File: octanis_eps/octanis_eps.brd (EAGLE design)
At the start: 100 x 80 mm, 167 parts, among them IC10 OPA2333DGK, IC11 OPA2333DGK, IC12 OPA2333DGK, IC2 OPA2333DGK, IC3 OPA2333DGK, IC4 OPA2333DGK, IC5 OPA2333DGK, IC6 OPA2333DGK, IC7 OPA2333DGK, IC8 OPA2333DGK, IC9 OPA2333DGK, Q1 FC-12M

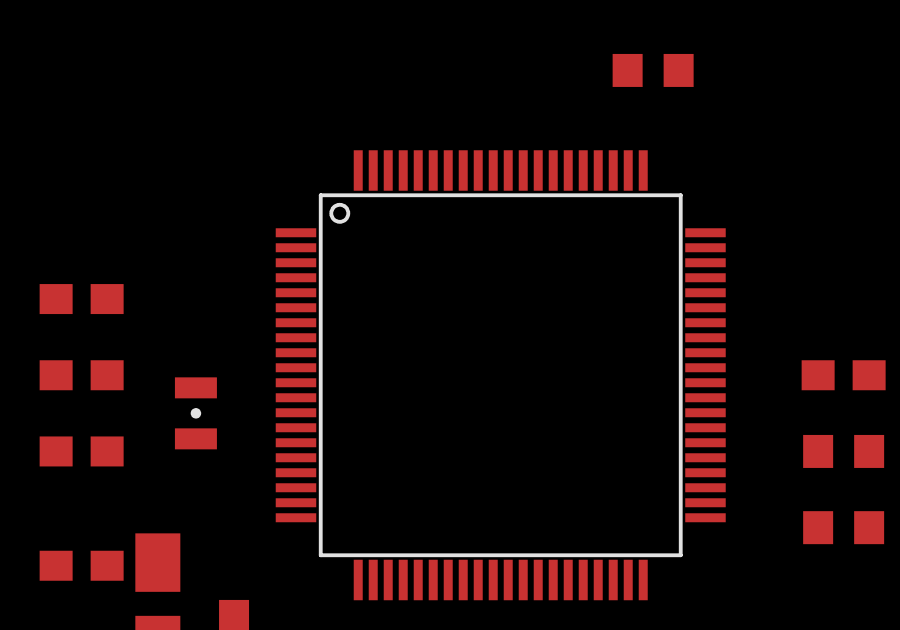
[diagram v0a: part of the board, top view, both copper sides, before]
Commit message: replaced the msp430 to the same component like in the octanis 0.1 board
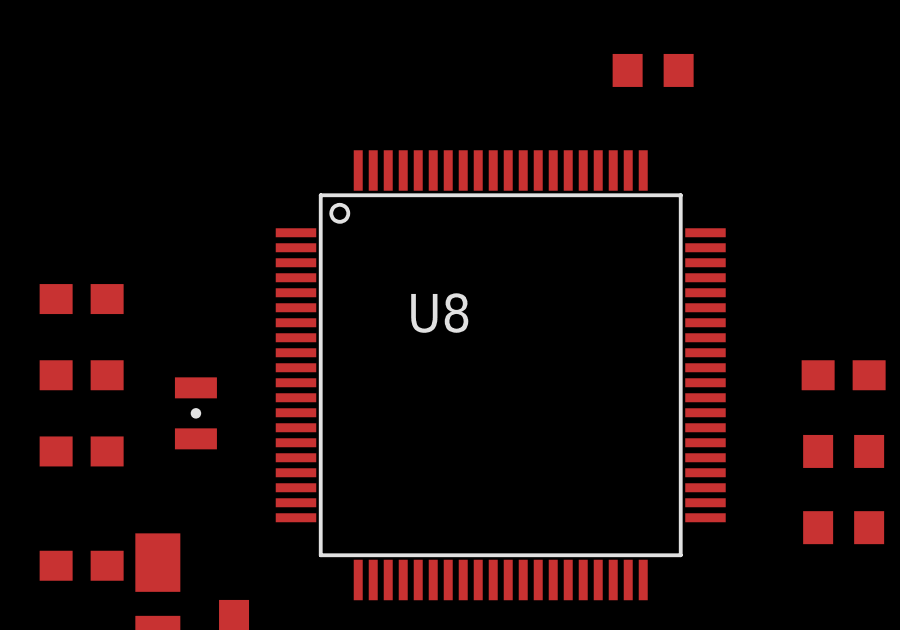
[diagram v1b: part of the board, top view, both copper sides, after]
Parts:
- removed U$1: F552X---PN80, TI_MSP430_v16:PN80
- added U8: MSP430F5529IPNR, TI_MSP430_v16_intern:PN80
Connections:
- net +3V3: now also U8.14, U8.18, U8.50; no longer U$1.14, U$1.18, U$1.50
- net 65: now also U8.65; no longer U$1.65
- net 66: now also U8.66; no longer U$1.66
- net 67: now also U8.67; no longer U$1.67
- net GND: now also U8.19, U8.49, U8.61, U8.68; no longer U$1.19, U$1.49, U$1.61, U$1.68
- net I2C_SCL: now also U8.47; no longer U$1.47
- net I2C_SDA: now also U8.46; no longer U$1.46
- net I_BOT_MS: now also U8.78; no longer U$1.78
- net I_CHG_MS: now also U8.79; no longer U$1.79
- net I_DSG_MS: now also U8.80; no longer U$1.80
- net I_TOP_MS: now also U8.77; no longer U$1.77
- net N$27: now also U8.63; no longer U$1.63
- net N$28: now also U8.45; no longer U$1.45
- net N$34: now also U8.3; no longer U$1.3
- net N$35: now also U8.4; no longer U$1.4
- net N$48: now also U8.12; no longer U$1.12
- net N$49: now also U8.20; no longer U$1.20
- net N$50: now also U8.13; no longer U$1.13
- net RST/SBWTDIO: now also U8.76; no longer U$1.76
- net TEST/SBWTCK: now also U8.71; no longer U$1.71
- net VCC: now also U8.11; no longer U$1.11
- net V_BT_MS: now also U8.2; no longer U$1.2
- net V_BUS_MS: now also U8.1; no longer U$1.1

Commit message: eps board save Thu-22-01-2015
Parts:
- removed EXT1, EXT2: (no value), jumper:JP4
- removed JP1, JP2, JP3, JP4, JP5: (no value), jumper:JP1
- removed U8: MSP430F5529IPNR, TI_MSP430_v16_intern:PN80
- added A_EXT, PW_EXT1, PW_EXT2, PW_EXT3, SC_JMPR: (no value), jumper:JP4
- added I2C: (no value), jumper:JP1
- added U$1: F552X---PN80, TI_MSP430_v16:PN80
- added U$16, U$17, U$18: TPS2022D, Octanis1_EPS:SO8
- moved U$15 508.6 mm to (54.6, 54.6), flipped to the bottom
- moved U$14 503.2 mm to (61.0, 54.6), flipped to the bottom
- moved U$13 492.2 mm to (48.3, 54.6), flipped to the bottom
- moved U$8 33.2 mm to (35.6, 33.0)
- moved LTC3411 30.9 mm to (80.0, 26.7)
- moved C17 30.5 mm to (91.4, 14.0)
- moved C9 21.6 mm to (81.3, 19.1)
- moved R68 17.3 mm to (83.8, 15.2)
- moved JP7 14.2 mm to (76.2, 76.2), turned to 0 degrees
- moved IC11 10.5 mm to (77.5, 12.7)
- moved IC10 9.67 mm to (80.0, 6.35)
- moved L1 8.98 mm to (88.9, 27.9)
- moved BT_JMPR 4.26 mm to (31.1, 72.4), turned to 90 degrees
- moved R10 3.81 mm to (38.1, 71.1)
- moved C7 1.80 mm to (29.2, 59.7)
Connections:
- removed net I_BOT_MS: IC3.6, IC3.7, U8.78
- removed net I_TOP_MS: IC3.1, IC3.2, U8.77
- removed net N$35: U8.4
- removed net SC+_BOT: R8.1, SC_BOT.1, SC_BOT.2, U$2.8
- removed net SC+_TOP: R6.1, SC_TOP.1, SC_TOP.2, U$3.8
- new net AEXT4: A_EXT.1, U$1.6
- new net A_EXT1: A_EXT.4, U$1.3
- new net A_EXT2: A_EXT.3, U$1.4
- new net A_EXT3: A_EXT.2, U$1.5
- new net EN_EXT1: U$1.57, U$13.1
- new net EN_EXT2: U$1.58, U$15.1
- new net EN_EXT3: U$1.59, U$14.1
- new net EXT3+: PW_EXT3.3, PW_EXT3.4, U$18.6, U$18.7, U$18.8
- new net EXT_PW: C26.+, C27.+, C28.+, C29.2, C30.2, C31.2, R6.2, U$16.2, U$16.3, U$17.2, U$17.3, U$18.2, U$18.3, U$3.6
- new net I_EXT_PW: IC3.1, IC3.2, U$1.78
- new net I_SC: IC3.6, IC3.7, U$1.77
- new net N$79: U$13.3, U$16.4
- new net N$80: U$14.3, U$18.4
- new net SC+: R8.1, SC_BOT.1, SC_BOT.2, SC_TOP.1, SC_TOP.2, U$2.8
- new net SC-: SC_BOT.3, SC_BOT.4, SC_JMPR.2, SC_JMPR.4, SC_TOP.3, SC_TOP.4
- net +3V3: now also U$1.14, U$1.18, U$1.50; no longer U8.14, U8.18, U8.50
- net 65: now also U$1.65; no longer U8.65
- net 66: now also U$1.66; no longer U8.66
- net 67: now also U$1.67; no longer U8.67
- net EXT1+: now also PW_EXT1.3, PW_EXT1.4, U$16.6, U$16.7, U$16.8; no longer EXT1.3, EXT1.4
- net EXT2+: now also PW_EXT2.3, PW_EXT2.4, U$17.6, U$17.7, U$17.8; no longer EXT2.3, EXT2.4
- net GND: now also C26.-, C27.-, C28.-, C29.1, C30.1, C31.1, PW_EXT1.1, PW_EXT1.2, PW_EXT2.1, PW_EXT2.2, PW_EXT3.1, PW_EXT3.2, SC_JMPR.1, SC_JMPR.3, U$1.19, U$1.49, U$1.61, U$1.68, U$16.1, U$17.1, U$18.1; no longer EXT1.1, EXT1.2, EXT2.1, EXT2.2, SC_BOT.3, SC_BOT.4, SC_TOP.3, SC_TOP.4, U8.19, U8.49, U8.61, U8.68
- net I2C_SCL: now also I2C.1, U$1.47; no longer JP1.1, U8.47
- net I2C_SDA: now also I2C.2, U$1.46; no longer JP1.2, U8.46
- net I_CHG_MS: now also U$1.79; no longer U8.79
- net I_DSG_MS: now also U$1.80; no longer U8.80
- net N$27: now also U$1.63; no longer U8.63
- net N$28: now also U$1.45; no longer U8.45
- net N$34: now also U$15.3, U$17.4; no longer U8.3
- net N$48: now also U$1.12; no longer U8.12
- net N$49: now also U$1.20; no longer U8.20
- net N$50: now also U$1.13; no longer U8.13
- net RST/SBWTDIO: now also U$1.76; no longer U8.76
- net TEST/SBWTCK: now also U$1.71; no longer U8.71
- net VCC: now also R6.1, U$1.11, U$3.8; no longer R6.2, U$3.6, U8.11
- net V_BT_MS: now also U$1.2; no longer U8.2
- net V_BUS_MS: now also U$1.1; no longer U8.1
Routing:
- net EXT_PW: track 0.00 -> 51.8 mm, vias 0 -> 1
- net SC-: track 0.00 -> 30.0 mm
- net SC+: track 0.00 -> 10.3 mm
- net BT_IN: track 2.54 -> 11.2 mm
- net GND: track 5.08 -> 0.00 mm
- net EXT3+: track 0.00 -> 5.08 mm
- net EXT2+: track 0.00 -> 5.08 mm
- net EXT1+: track 0.00 -> 5.08 mm
- net VCC: track 254.7 -> 249.6 mm, vias 4 -> 3
- net BT+: track 17.3 -> 13.5 mm
- net BT-: track 15.0 -> 18.2 mm
- net SC+_TOP: track 2.54 -> 0.00 mm
- net SC+_BOT: track 2.54 -> 0.00 mm
